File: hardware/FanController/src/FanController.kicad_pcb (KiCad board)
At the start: 2 copper layers, 51 x 12 mm, 13 parts, among them J1 MC 1,5/2, J2 Fan, J3 Fan, J4 Fan, U1 12F1501, U2 MCP9700T

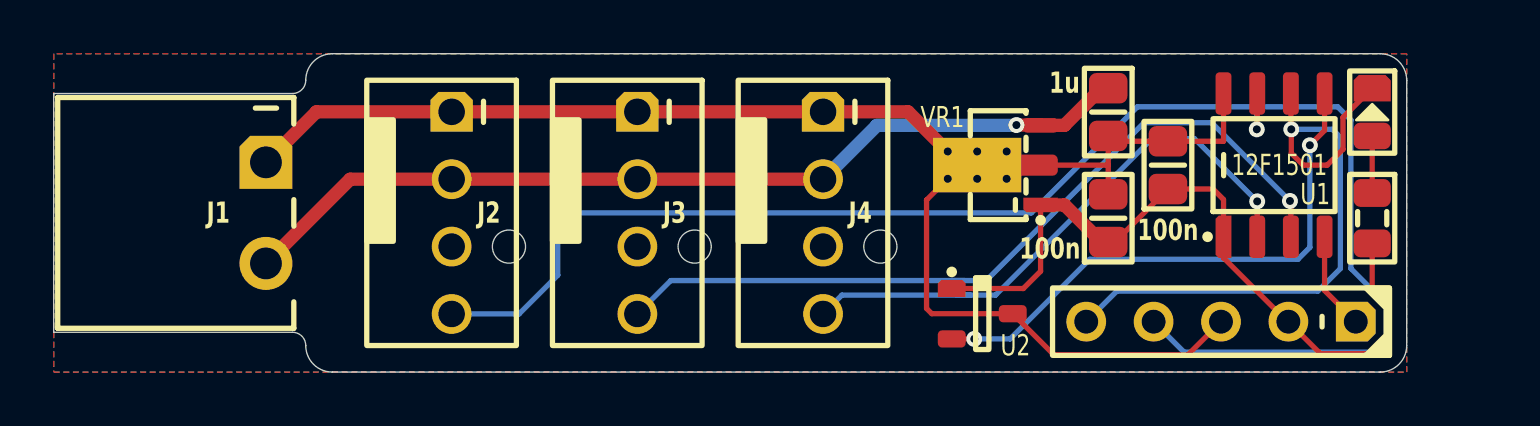
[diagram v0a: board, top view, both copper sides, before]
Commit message: Fancontroller supports 4 fans
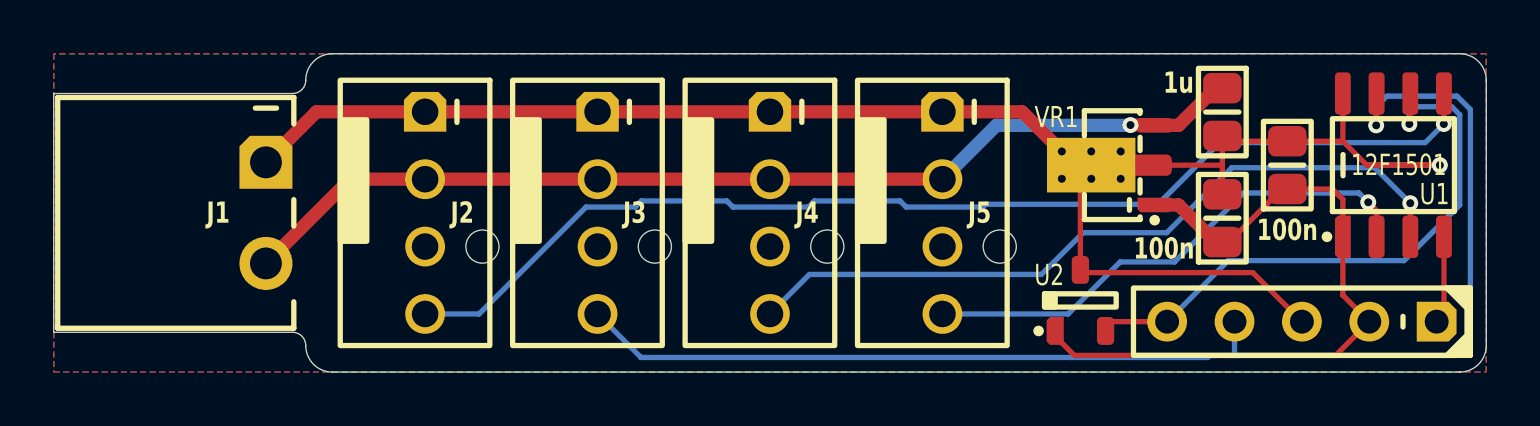
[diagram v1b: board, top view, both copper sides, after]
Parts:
- removed DS1: LED, Medo64:DS (0805)
- removed R1: 10K, Medo64:R (0805)
- added J4: Fan, Medo64:J Molex 047053 [Fan] (4w), F.Cu at (42.0, 21.0)
- moved C1 4.50 mm to (61.5, 19.2)
- moved J5 4.50 mm to (48.5, 21.0)
- moved U1 4.50 mm to (65.5, 19.2)
- moved C2 4.30 mm to (59.0, 21.2)
- moved C3 4.30 mm to (59.0, 17.2)
- moved VR1 4.30 mm to (56.5, 19.2)
- moved U2 3.73 mm to (53.7, 24.3), turned to 0 degrees
- moved ICSP 3.05 mm to (62.0, 25.1)
- moved J3 1.50 mm to (35.5, 21.0)
- moved J2 1.00 mm to (29.0, 21.0)
- renumbered J4 to J5
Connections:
- ICSP pad 4: PWM1 -> PWM2
- ICSP pad 5: LED -> TEMPERATURE
- J5 pad 4: PWM3 -> PWM4
- U1 pad 2: PWM3 -> PWM4
- U1 pad 3: PWM2 -> PWM3
- U1 pad 5: TEMPERATURE -> PWM1
- U1 pad 6: LED -> TEMPERATURE
- U1 pad 7: PWM1 -> PWM2
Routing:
- net LED: track 24.7 -> 0.00 mm, vias 1 -> 0
- net PWM4: track 0.00 -> 19.5 mm, vias 0 -> 1
- net PWM2: track 30.7 -> 49.7 mm
- net PWM1: track 58.8 -> 42.9 mm
- net PWM3: track 21.9 -> 28.2 mm
- net GND: track 64.4 -> 69.3 mm, vias 0 -> 1
- net 12V: track 34.5 -> 38.5 mm
- net 5V: track 28.6 -> 25.7 mm
- net LED': track 2.15 -> 0.00 mm
- net TEMPERATURE: track 21.0 -> 22.3 mm, vias 2 -> 1
- net ICSP_VPP: track 3.69 -> 2.93 mm
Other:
- board size 51 x 12 mm -> 54 x 12 mm

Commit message: Added FanController schematics
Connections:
- net 12V renamed +12V

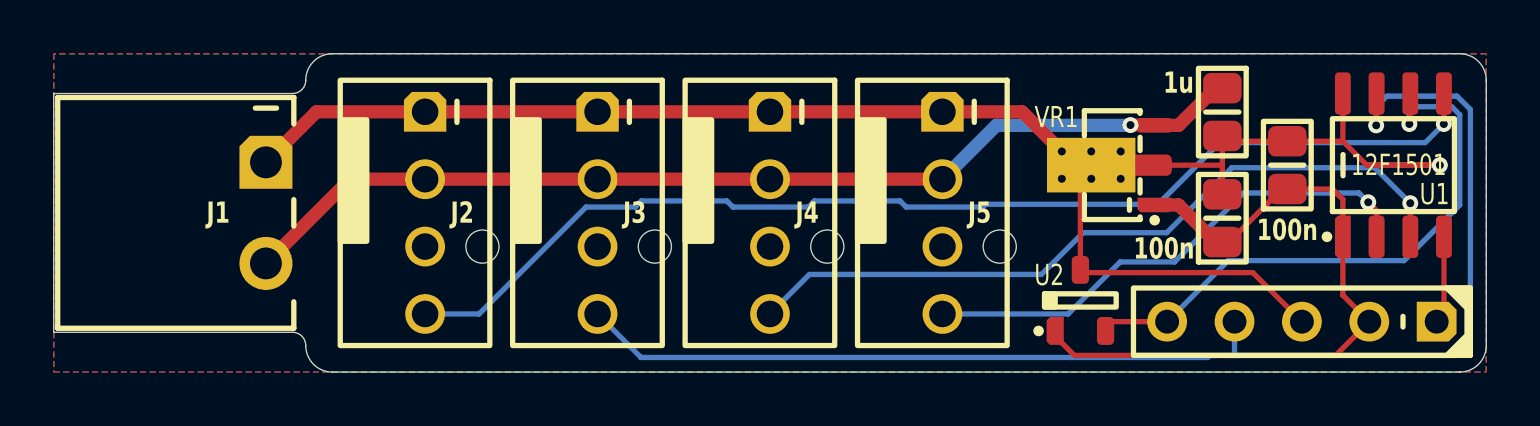
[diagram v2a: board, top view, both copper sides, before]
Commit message: Replaced MCP9700A with MCP9701A
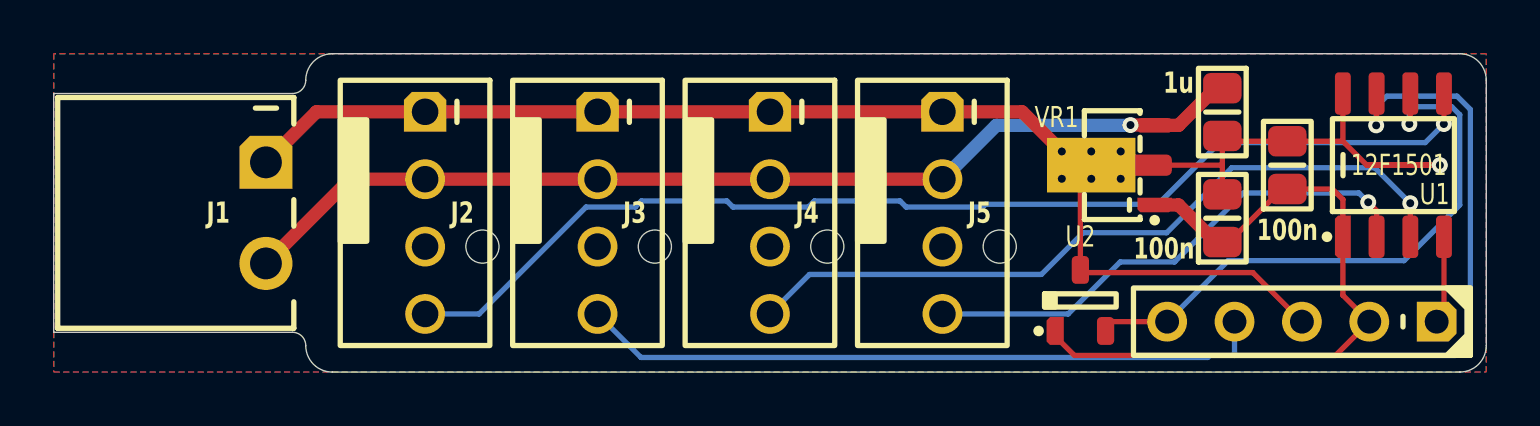
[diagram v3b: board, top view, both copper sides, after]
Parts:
- U2: value MCP9700T -> MCP9701A; footprint Medo64:U Temperature Analog [MCP9700T] (SOT23-3) -> Medo64:U Temperature Analog [MCP9701] (SOT23-3)
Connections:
- net 5V renamed +5V
- net PWM1 renamed OUT_PWM1
- net PWM2 renamed OUT_PWM2
- net PWM3 renamed OUT_PWM3
- net PWM4 renamed OUT_PWM4
- net TEMPERATURE renamed ADC_TEMPERATURE
